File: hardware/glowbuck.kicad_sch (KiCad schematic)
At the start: 55 parts, among them J1 Conn_01x04_Socket, J105 Conn_01x01_Pin, J106 Conn_01x01_Pin, J107 Conn_01x01_Pin, J3 Conn_02x08_Counter_Clockwise, SW101 SW_Push, SW102 SW_Push, U101 ESP32-S3-WROOM-1, U102 SN74LVC1T45DBV, U103 INA181A3

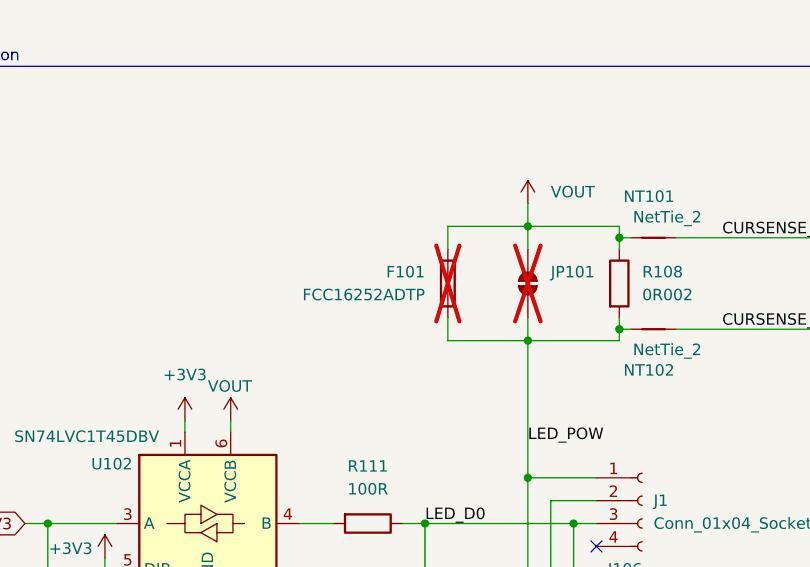
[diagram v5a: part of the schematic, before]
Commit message: Layout Stecker final, USB done, buck wip
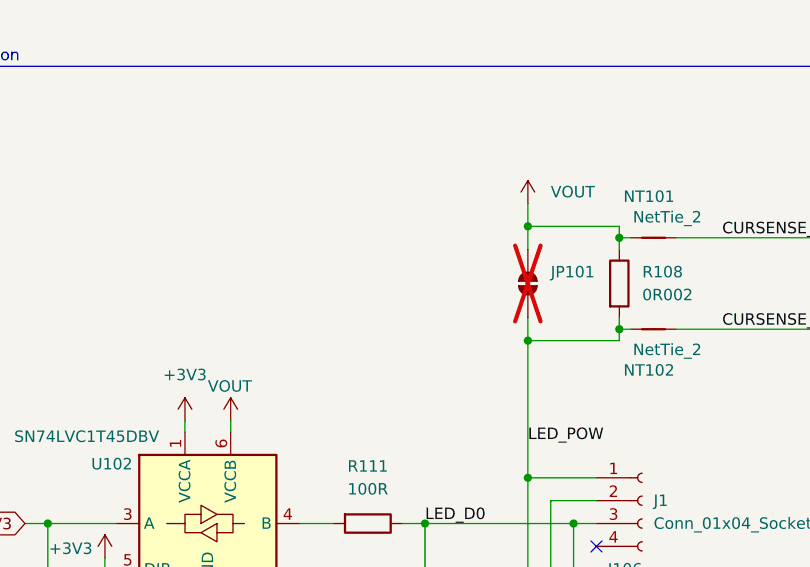
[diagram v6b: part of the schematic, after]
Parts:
- removed F101: FCC16252ADTP, Fuse:Fuse_0603_1608Metric, symbol Device:Fuse
- J3: footprint Connector_PinHeader_2.54mm:PinHeader_2x08_P2.54mm_Vertical -> Connector_PinHeader_2.00mm:PinHeader_2x08_P2.00mm_Vertical; MouserNumber 649-1012938391601ALF -> (none)

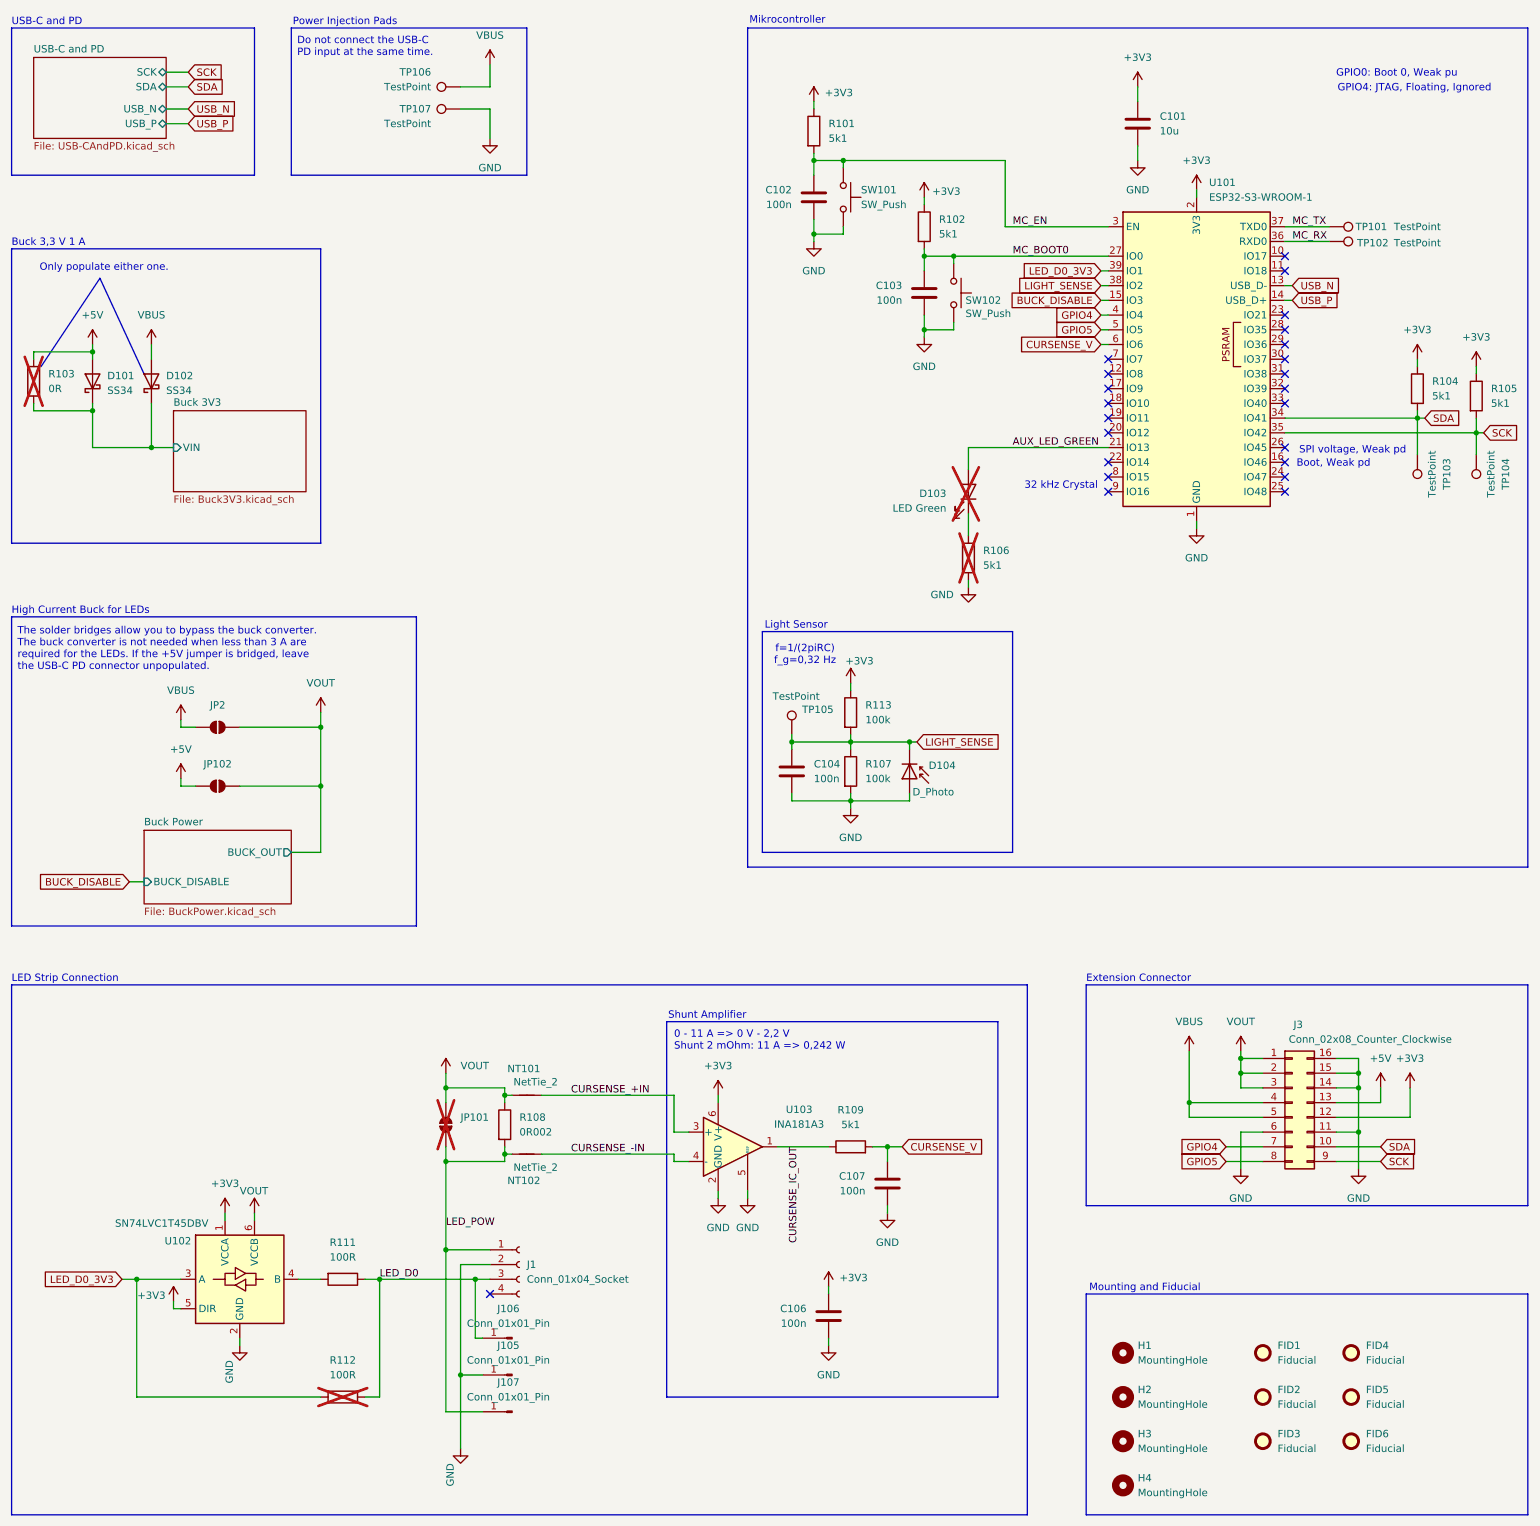
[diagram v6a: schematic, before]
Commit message: Layout in progress. I2C done
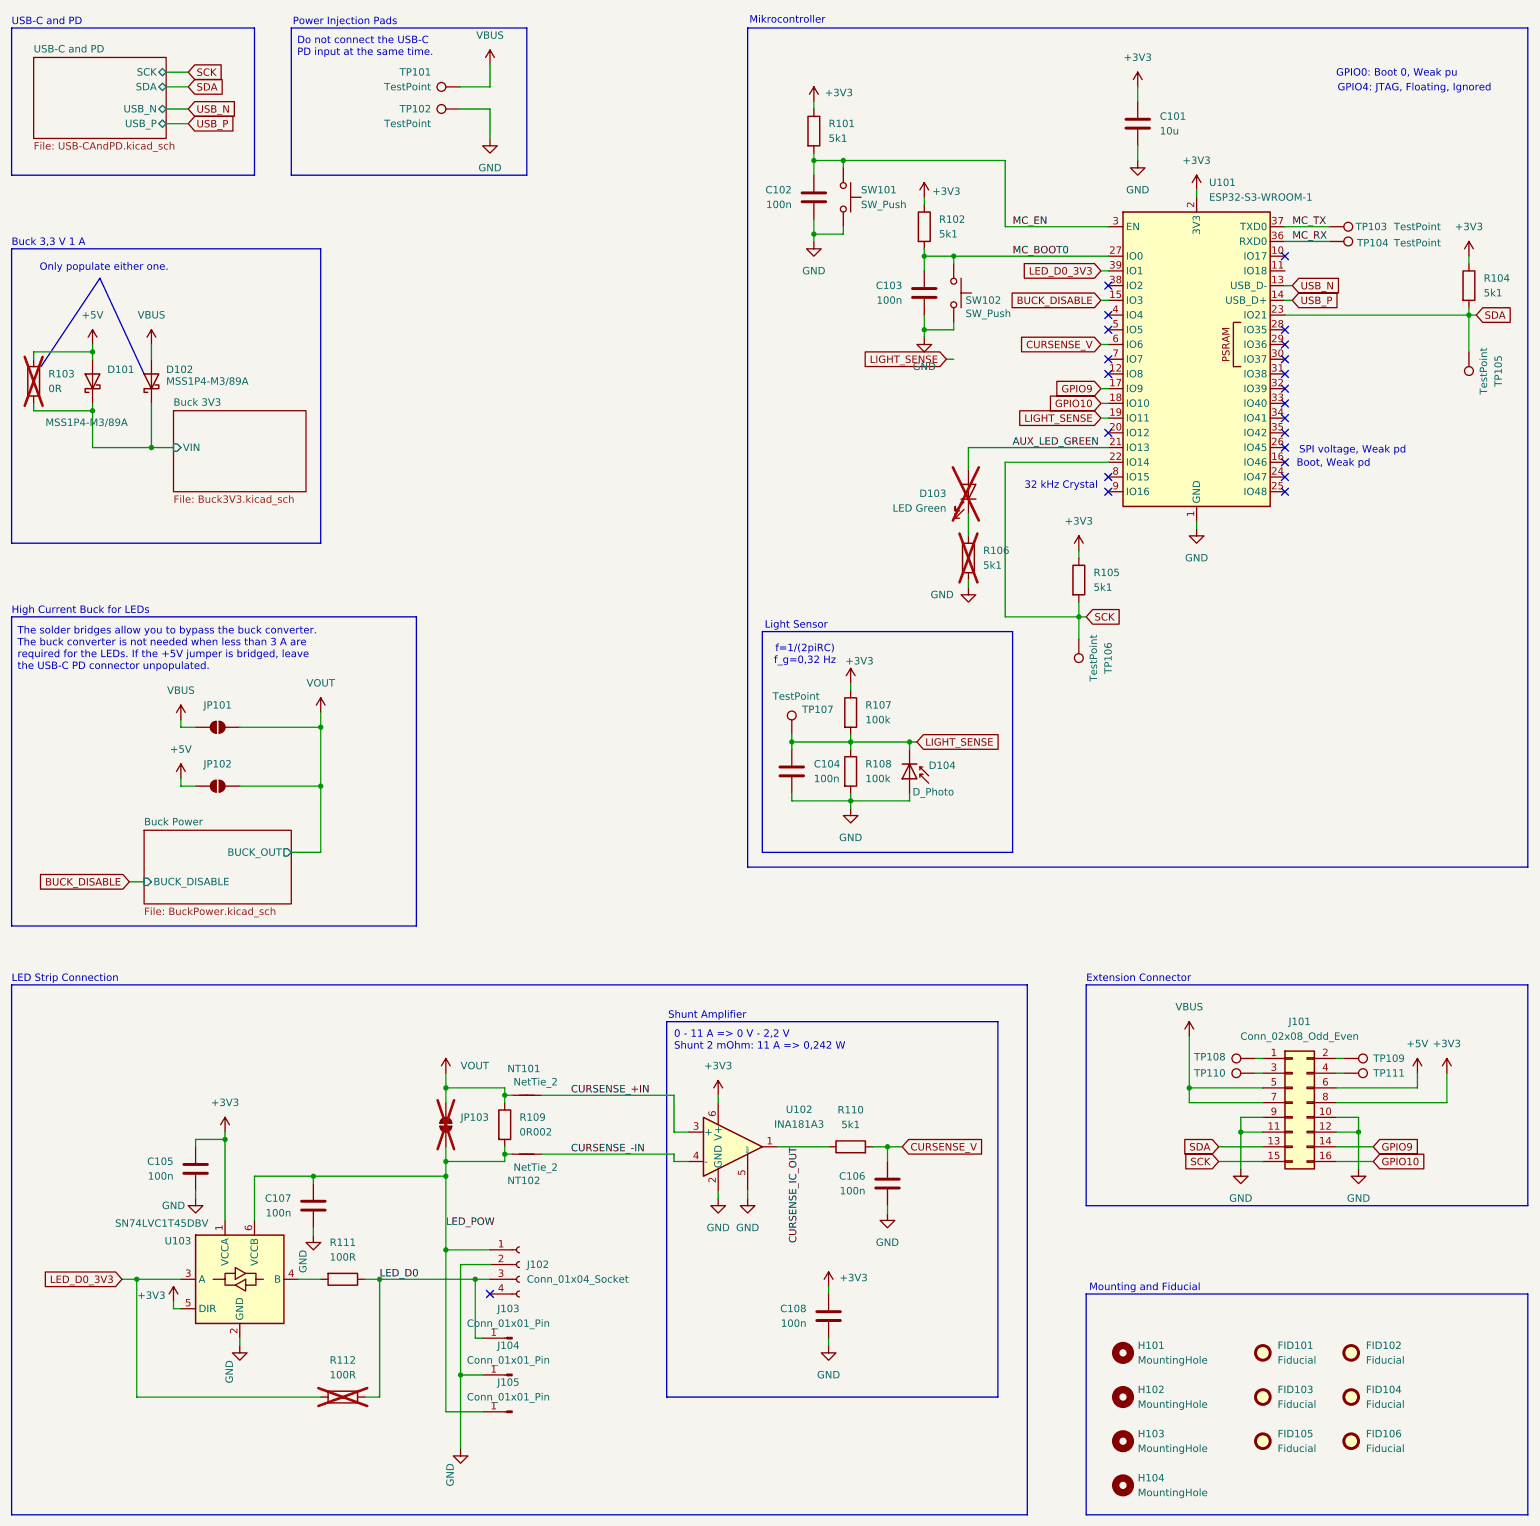
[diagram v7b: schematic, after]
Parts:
- removed D101, D102: SS34, Diode_SMD:D_SMA, symbol Diode:SS34
- removed J3: Conn_02x08_Counter_Clockwise, Connector_PinHeader_2.00mm:PinHeader_2x08_P2.00mm_Vertical, symbol Connector_Generic:Conn_02x08_Counter_Clockwise
- added C105, C107: 100n, Capacitor_SMD:C_0603_1608Metric, symbol Device:C
- added D101, D102: MSS1P4-M3/89A, Diode_SMD:D_MicroSMP_AK, symbol Device:D_Schottky
- added J101: Conn_02x08_Odd_Even, Connector_PinHeader_2.00mm:PinHeader_2x08_P2.00mm_Vertical, symbol Connector_Generic:Conn_02x08_Odd_Even
- added TP108, TP109, TP110, TP111: TestPoint, TestPoint:TestPoint_Pad_D1.0mm, symbol Connector:TestPoint
- J103: renamed from J106; footprint TestPoint:TestPoint_Pad_2.0x2.0mm -> TestPoint:TestPoint_Pad_1.0x1.0mm
- renumbered C107 to C106, C106 to C108, FID1 to FID101, FID4 to FID102, FID2 to FID103, FID5 to FID104, FID3 to FID105, FID6 to FID106, H1 to H101, H2 to H102, H3 to H103, H4 to H104, J1 to J102, J105 to J104, J107 to J105, JP2 to JP101, JP101 to JP103, R113 to R107, R107 to R108, R108 to R109, R109 to R110, TP106 to TP101, TP107 to TP102, TP101 to TP103, TP102 to TP104, TP103 to TP105, TP104 to TP106, TP105 to TP107, U103 to U102, U102 to U103
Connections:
- net +3V3: now also C105.1, J101.8 (Pin_8)
- net +5V: now also D101.2 (A), J101.6 (Pin_6)
- net Buck 3V3/VIN: now also D101.1 (K), D102.1 (K)
- net GND: now also C105.2, C107.2, J101.10 (Pin_10), J101.11 (Pin_11), J101.12 (Pin_12), J101.9 (Pin_9)
- net LED_POW: now also U103.6 (VCCB), C107.1
- net LIGHT_SENSE: now also U101.19 (IO11); no longer U101.38 (IO2)
- net SCK: now also U101.22 (IO14), J101.15 (Pin_15); no longer U101.35 (IO42)
- net SDA: now also U101.23 (IO21), J101.13 (Pin_13); no longer U101.34 (IO41)
- net VBUS: now also D102.2 (A), J101.5 (Pin_5), J101.7 (Pin_7)
- net VOUT: no longer U103.6 (VCCB)
- net GPIO9: now reaches U101.17 (IO9)
- net GPIO9: now also J101.14 (Pin_14)
- net GPIO10: now reaches U101.18 (IO10)
- net GPIO10: now also J101.16 (Pin_16)
- net GPIO4: no longer names the net of U101.4 (IO4)
- net GPIO5: no longer names the net of U101.5 (IO5)
- new net: J101.3 (Pin_3), TP110.1
- new net: J101.1 (Pin_1), TP108.1
- new net: J101.2 (Pin_2), TP109.1
- new net: J101.4 (Pin_4), TP111.1
- no-connect marks 23 -> 22
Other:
- moved on the sheet: R104, R105, TP105, TP106

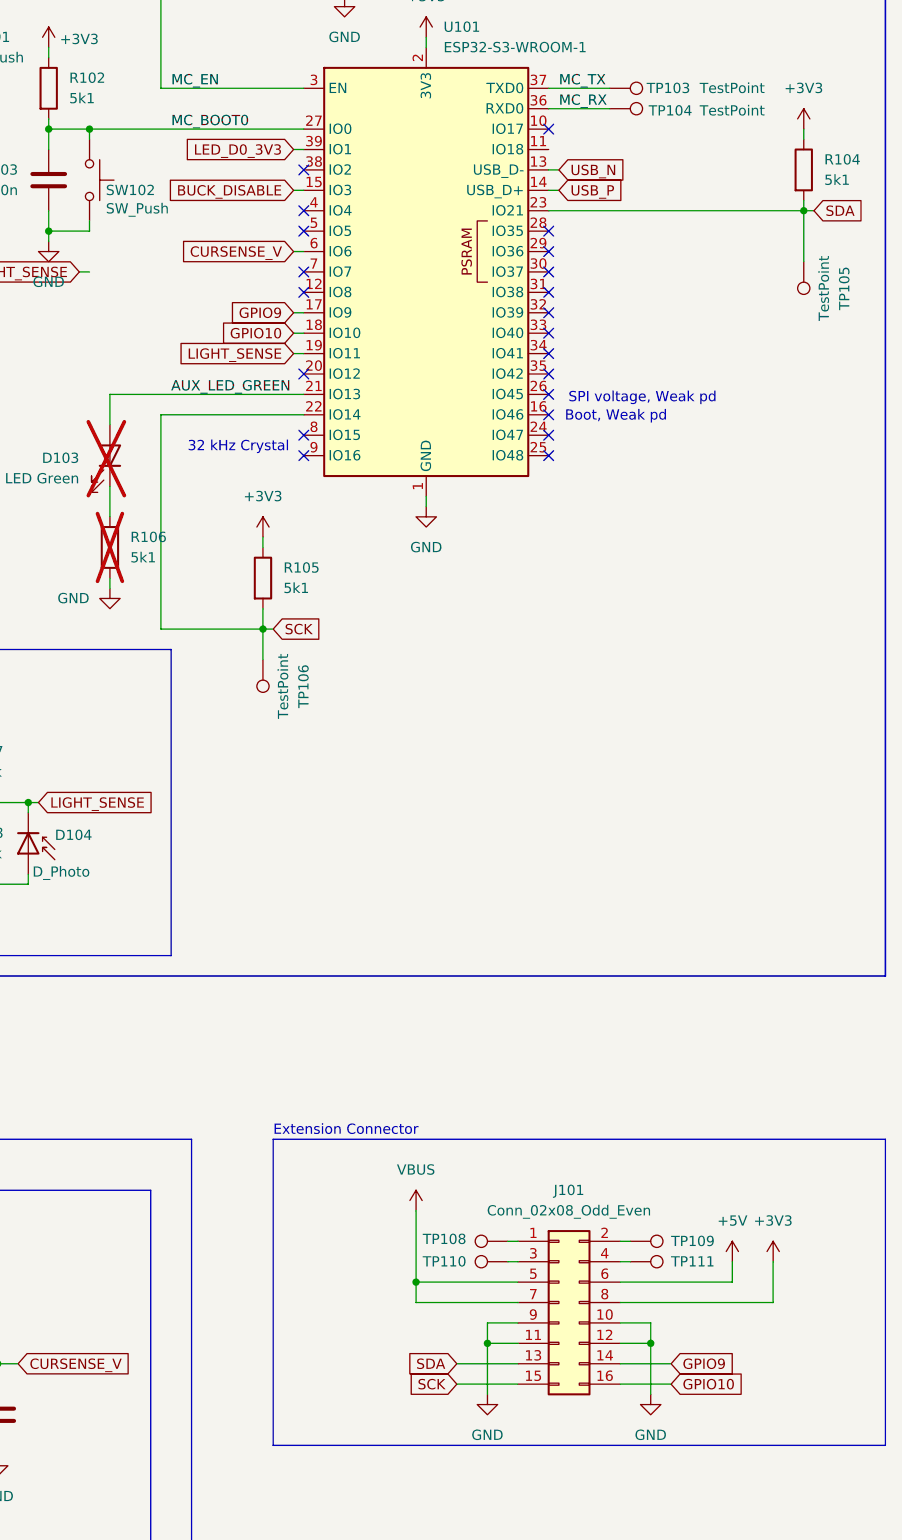
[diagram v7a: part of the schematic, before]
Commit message: Fixed drc errors
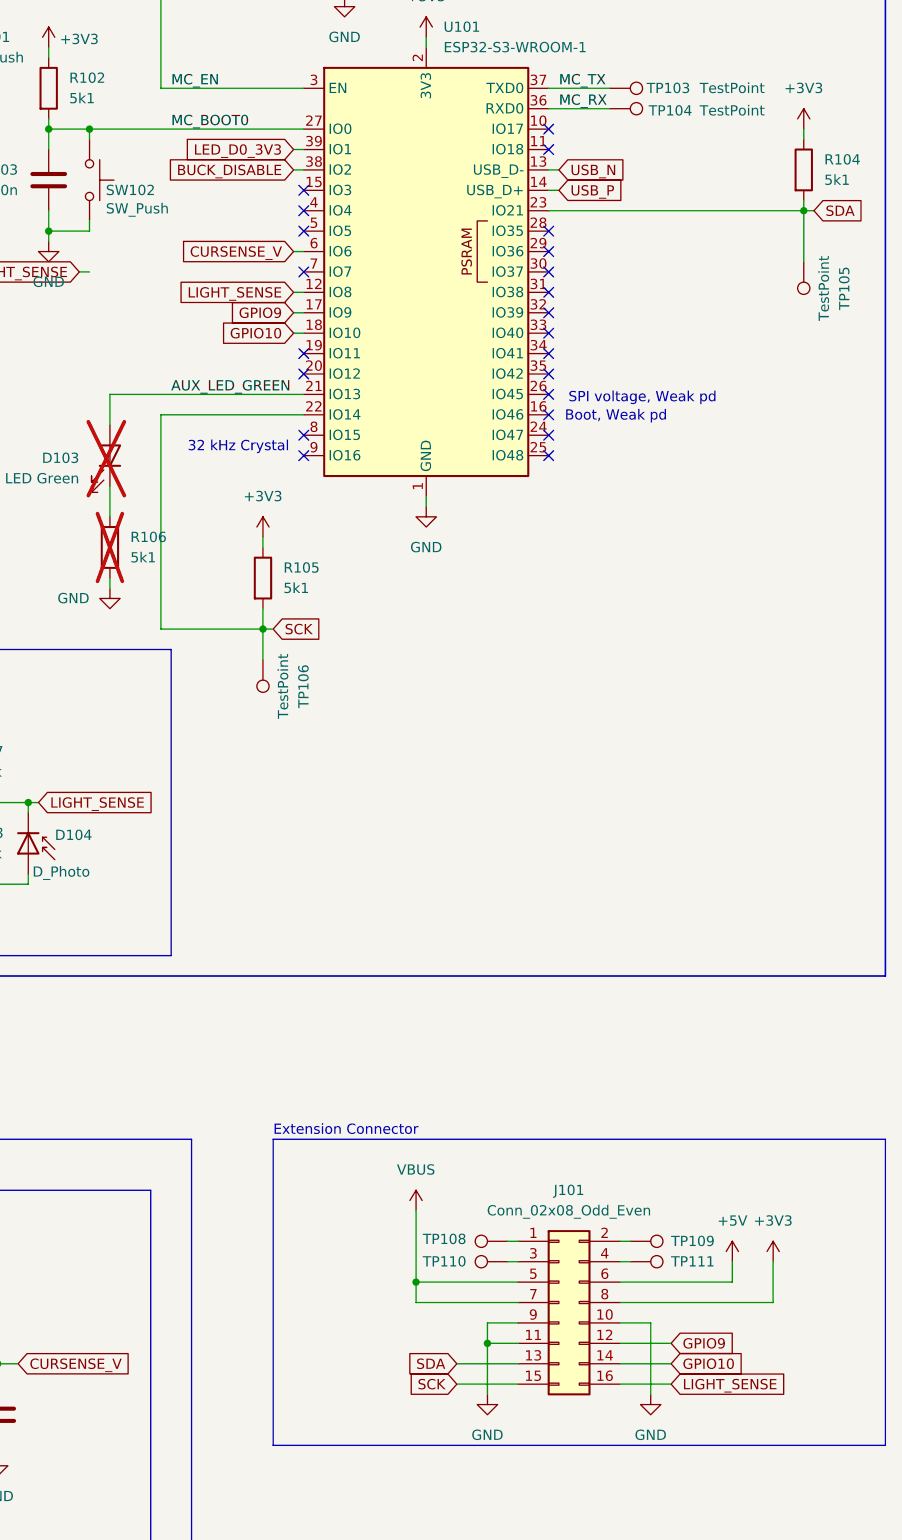
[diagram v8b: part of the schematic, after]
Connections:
- net BUCK_DISABLE: now also U101.38 (IO2); no longer U101.15 (IO3)
- net GND: no longer J101.12 (Pin_12)
- net GPIO10: now also J101.14 (Pin_14); no longer J101.16 (Pin_16)
- net GPIO9: now also J101.12 (Pin_12); no longer J101.14 (Pin_14)
- net LIGHT_SENSE: now also J101.16 (Pin_16), U101.12 (IO8); no longer U101.19 (IO11)
- no-connect marks 22 -> 23
